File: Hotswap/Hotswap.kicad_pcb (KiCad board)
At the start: 4 copper layers, 41.5 x 75.5 mm, 18 parts, among them J1 XT90PW-F, J2 XT90PW-F, J3 XT90PW-M, Q11 2N3904, Q2 IRFP4468PbF, Q4 IRFP4468PbF, Q8 IRFP4468PbF, Q9 IRFP4468PbF, U2 LM74800QDRRRQ1, U5 LM74800QDRRRQ1

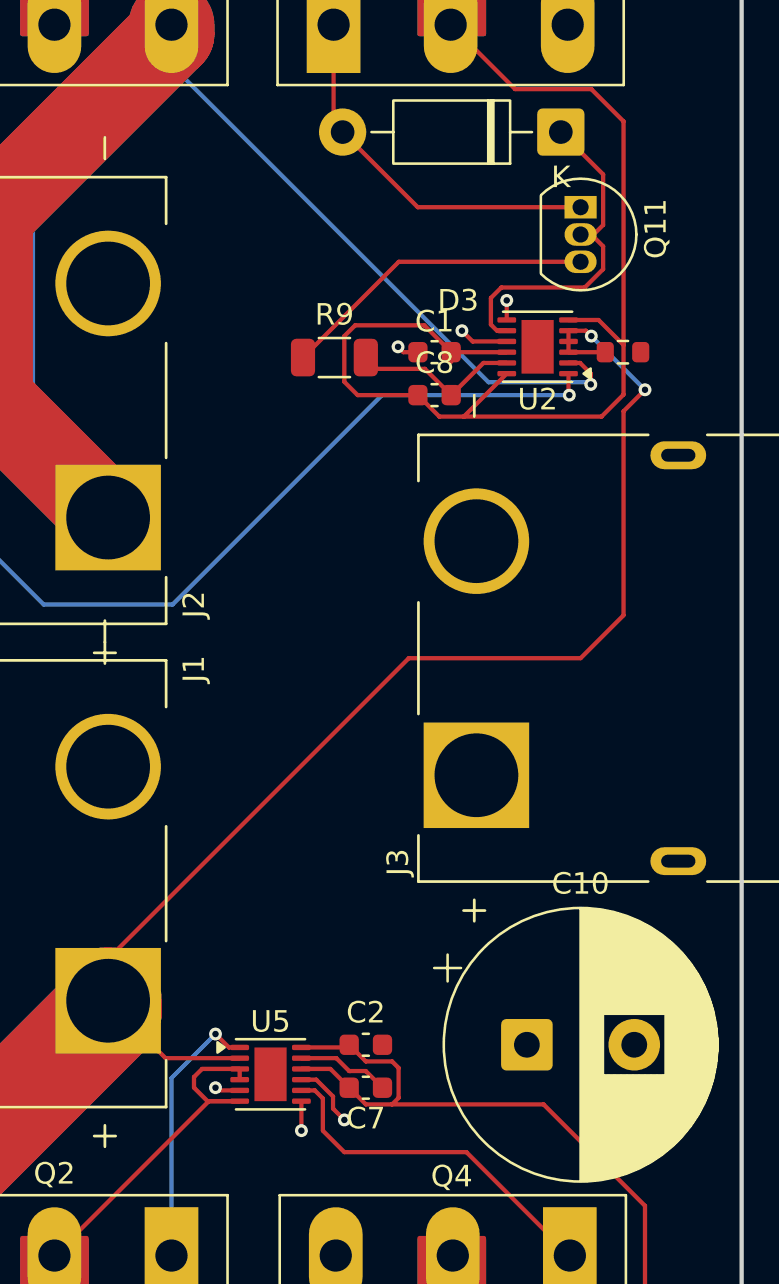
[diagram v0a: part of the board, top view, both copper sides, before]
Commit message: update MOSFET to IRF7430
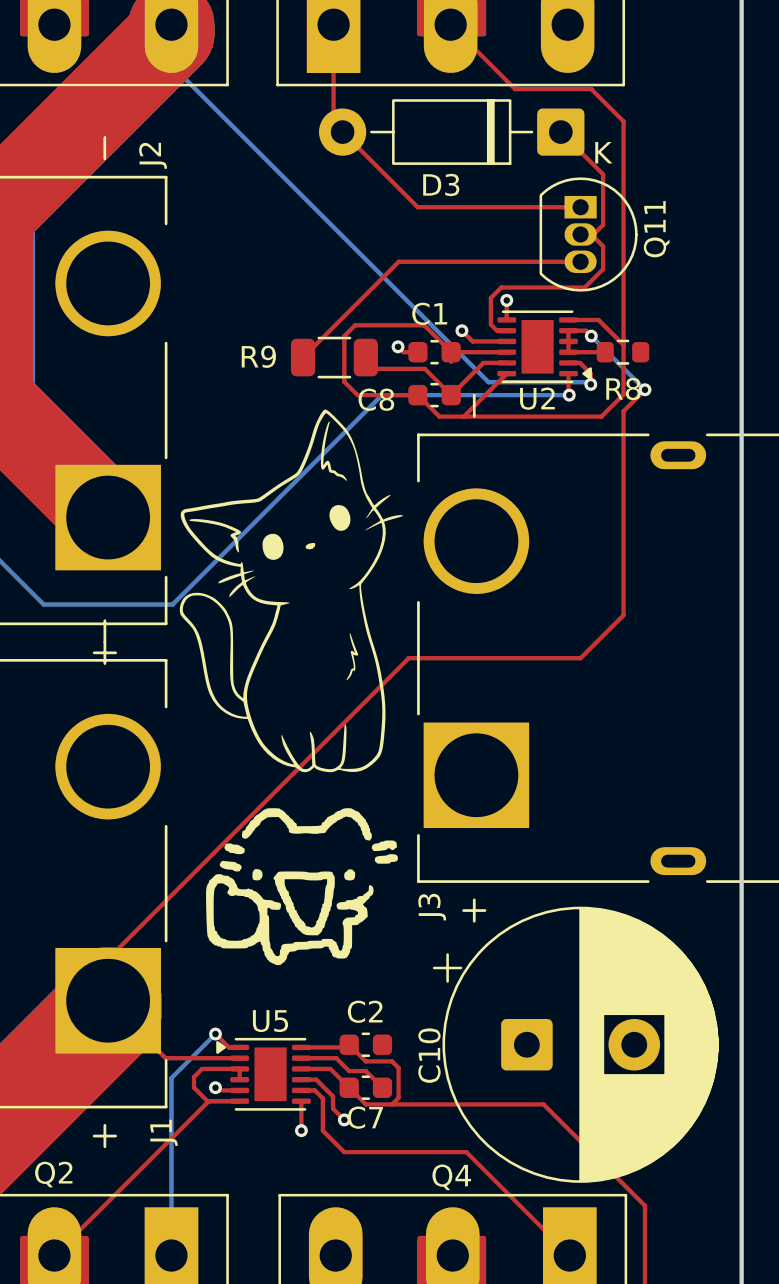
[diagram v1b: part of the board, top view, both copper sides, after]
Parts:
- added G***: LOGO, LOGO, F.Cu at (66.0, 54.0)
- added G***: LOGO, LOGO, F.Cu at (66.0, 67.5)
- Q2, Q4, Q8, Q9: value IRFP4468PbF -> IRFP7430PBF
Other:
- board text added: "C1"
- board text added: "R8"
- board text added: "TORO HOTSWAP v0.1"
